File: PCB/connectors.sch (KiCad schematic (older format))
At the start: 54 parts, among them J10 70543-0002, J11 70543-0002, J12 70543-0002, J13 70543-0002, J14 Conn_02x05_Odd_Even, J15 Conn_02x05_Odd_Even, J16 70543-0001, J17 70543-0001, J18 70543-0001, J19 Conn_02x05_Odd_Even, J20 62201021121, J21 70543-0001, J22 70543-0001, J7 USB_B, J8 70543-0002, J9 70543-0002, U10 TXB0108PWR, U11 TXB0108PWR, U12 TXB0108PWR, U13 TXB0108PWR

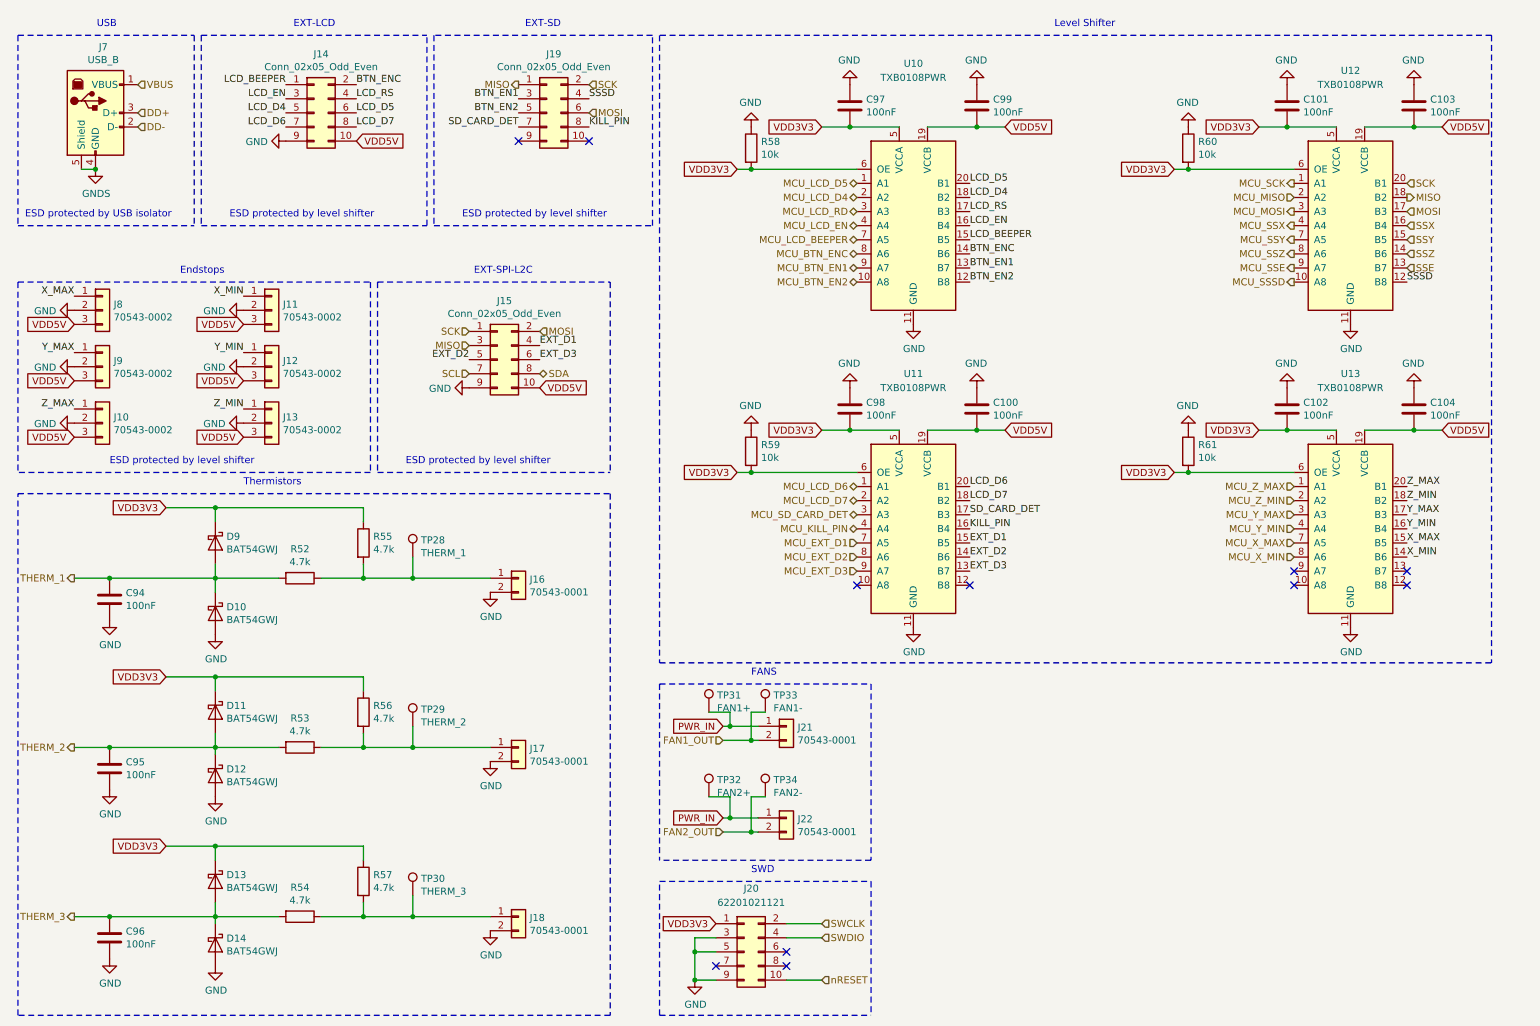
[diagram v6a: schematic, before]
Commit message: Saving work in progress.
Every component now has a 3D mode.
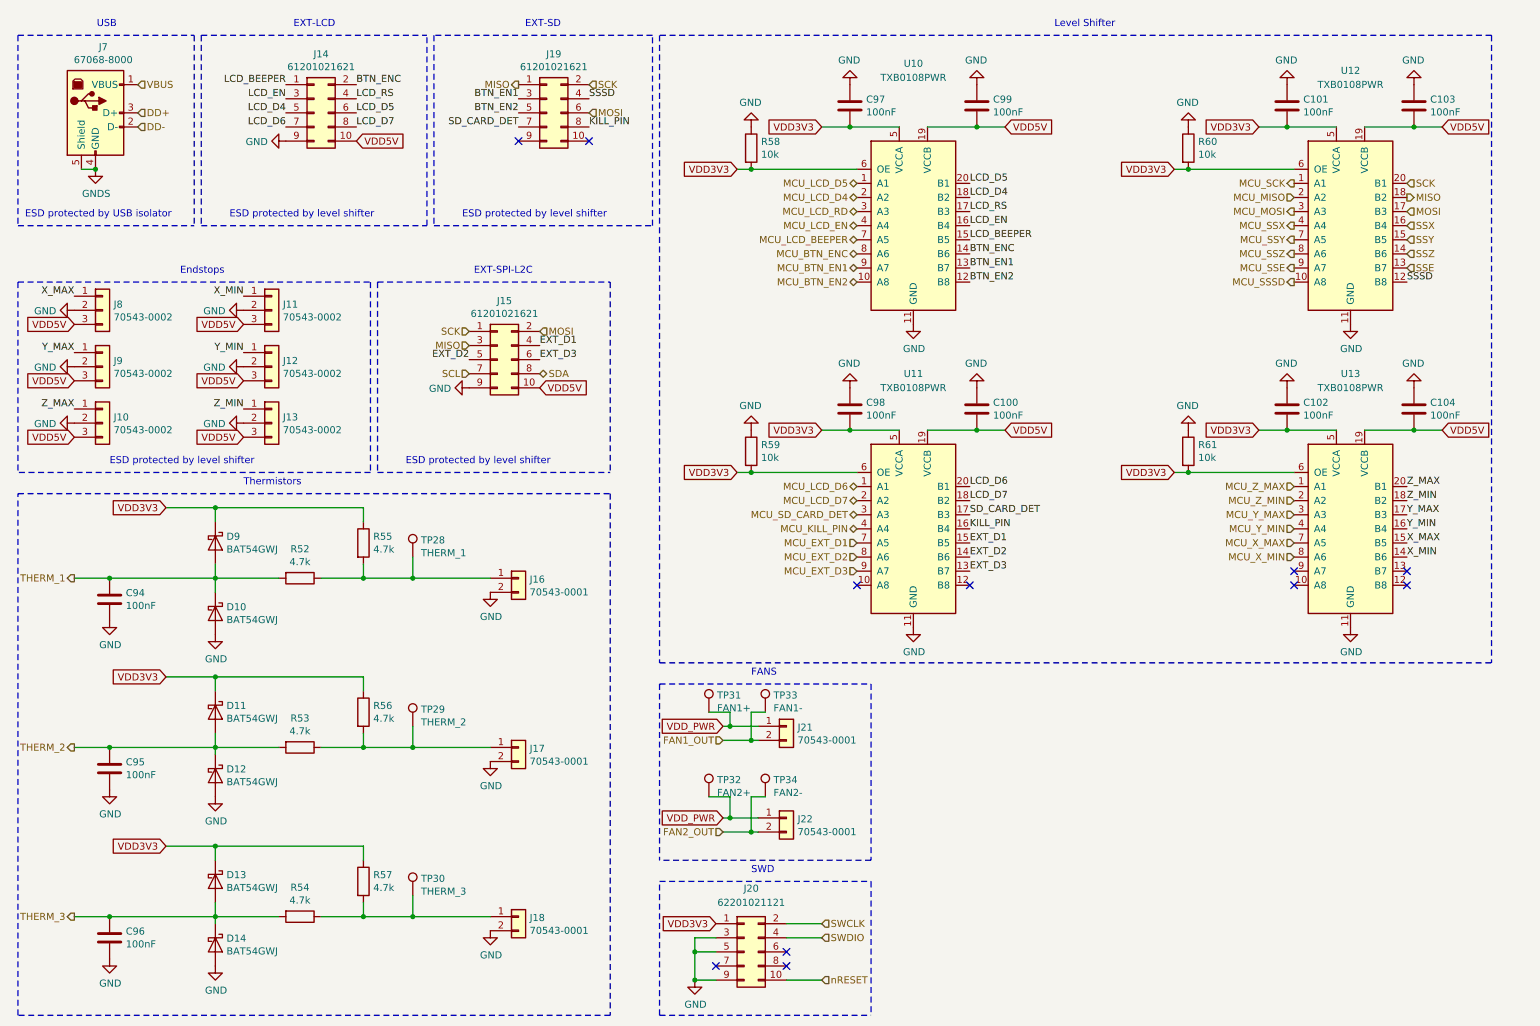
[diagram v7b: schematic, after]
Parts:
- J10, J11, J12, J13, J8, J9: footprint Connector_PinHeader_2.54mm:PinHeader_1x03_P2.54mm_Vertical -> custom-footprints:70543-0002
- J14, J15, J19: value Conn_02x05_Odd_Even -> 61201021621; footprint Connector_PinHeader_2.54mm:PinHeader_2x05_P2.54mm_Vertical -> custom-footprints:Box_Header_2x05x2.54mm_Straight
- J16, J17, J18, J21, J22: footprint Connector_PinHeader_2.54mm:PinHeader_1x02_P2.54mm_Vertical -> custom-footprints:70543-0001
- J7: value USB_B -> 67068-8000; footprint Connector_USB:USB_B_TE_5787834_Vertical -> custom-footprints:67068-8000
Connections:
- net PWR_IN renamed VDD_PWR
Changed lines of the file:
@@
 P 1150 1300
 F 0 "J7" H 1205 1767 50  0000 C CNN
-F 1 "USB_B" H 1205 1676 50  0000 C CNN
-F 2 "Connector_USB:USB_B_TE_5787834_Vertical" H 1300 1250 50  0001 C CNN
-F 3 "https://www.mouser.de/ProductDetail/TE-Connectivity/5787834-1?qs=sGAEpiMZZMulM8LPOQ%252bykzAp4yt8IxVbCJriWtalJzg%3d" H 1300 1250 50  0001 C CNN
+F 1 "67068-8000" H 1205 1676 50  0000 C CNN
+F 2 "custom-footprints:67068-8000" H 1300 1250 50  0001 C CNN
+F 3 "https://www.mouser.de/datasheet/2/276/0670688000_IO_CONNECTORS-172066.pdf" H 1300 1250 50  0001 C CNN
 	1    1150 1300
 	1    0    0    -1
@@
 P 2700 1300
 F 0 "J14" H 2750 1717 50  0000 C CNN
-F 1 "Conn_02x05_Odd_Even" H 2750 1626 50  0000 C CNN
-F 2 "Connector_PinHeader_2.54mm:PinHeader_2x05_P2.54mm_Vertical" H 2700 1300 50  0001 C CNN
-F 3 "~" H 2700 1300 50  0001 C CNN
+F 1 "61201021621" H 2750 1626 50  0000 C CNN
+F 2 "custom-footprints:Box_Header_2x05x2.54mm_Straight" H 2700 1300 50  0001 C CNN
+F 3 "https://www.mouser.de/ProductDetail/Wurth-Electronics/61201021621?qs=%2fha2pyFadugkhyfdWLPRIwz9kroMfF%252bXZWEETFcVSqiQRaqHzEC2RQ%3d%3d" H 2700 1300 50  0001 C CNN
 	1    2700 1300
 	1    0    0    -1
@@
 P 4350 1300
 F 0 "J19" H 4400 1717 50  0000 C CNN
-F 1 "Conn_02x05_Odd_Even" H 4400 1626 50  0000 C CNN
-F 2 "Connector_PinHeader_2.54mm:PinHeader_2x05_P2.54mm_Vertical" H 4350 1300 50  0001 C CNN
-F 3 "~" H 4350 1300 50  0001 C CNN
+F 1 "61201021621" H 4400 1626 50  0000 C CNN
+F 2 "custom-footprints:Box_Header_2x05x2.54mm_Straight" H 4350 1300 50  0001 C CNN
+F 3 "https://www.mouser.de/ProductDetail/Wurth-Electronics/61201021621?qs=%2fha2pyFadugkhyfdWLPRIwz9kroMfF%252bXZWEETFcVSqiQRaqHzEC2RQ%3d%3d" H 4350 1300 50  0001 C CNN
 	1    4350 1300
 	1    0    0    -1
@@
 P 4000 3050
 F 0 "J15" H 4050 3467 50  0000 C CNN
-F 1 "Conn_02x05_Odd_Even" H 4050 3376 50  0000 C CNN
-F 2 "Connector_PinHeader_2.54mm:PinHeader_2x05_P2.54mm_Vertical" H 4000 3050 50  0001 C CNN
-F 3 "~" H 4000 3050 50  0001 C CNN
+F 1 "61201021621" H 4050 3376 50  0000 C CNN
+F 2 "custom-footprints:Box_Header_2x05x2.54mm_Straight" H 4000 3050 50  0001 C CNN
+F 3 "https://www.mouser.de/ProductDetail/Wurth-Electronics/61201021621?qs=%2fha2pyFadugkhyfdWLPRIwz9kroMfF%252bXZWEETFcVSqiQRaqHzEC2RQ%3d%3d" H 4000 3050 50  0001 C CNN
 	1    4000 3050
 	1    0    0    -1
@@
 F 0 "J16" H 4229 4592 50  0000 L CNN
 F 1 "70543-0001" H 4229 4501 50  0000 L CNN
-F 2 "Connector_PinHeader_2.54mm:PinHeader_1x02_P2.54mm_Vertical" H 4150 4600 50  0001 C CNN
+F 2 "custom-footprints:70543-0001" H 4150 4600 50  0001 C CNN
 F 3 "https://www.mouser.de/ProductDetail/Molex/50-57-9402?qs=%2fha2pyFadujDsSJKPzBRyOySofHgnbNURyOy7MwFkp4%3d" H 4150 4600 50  0001 C CNN
 	1    4150 4600
@@
 F 0 "J17" H 4229 5792 50  0000 L CNN
 F 1 "70543-0001" H 4229 5701 50  0000 L CNN
-F 2 "Connector_PinHeader_2.54mm:PinHeader_1x02_P2.54mm_Vertical" H 4150 5800 50  0001 C CNN
+F 2 "custom-footprints:70543-0001" H 4150 5800 50  0001 C CNN
 F 3 "https://www.mouser.de/ProductDetail/Molex/50-57-9402?qs=%2fha2pyFadujDsSJKPzBRyOySofHgnbNURyOy7MwFkp4%3d" H 4150 5800 50  0001 C CNN
 	1    4150 5800
@@
 F 0 "J18" H 4229 6992 50  0000 L CNN
 F 1 "70543-0001" H 4229 6901 50  0000 L CNN
-F 2 "Connector_PinHeader_2.54mm:PinHeader_1x02_P2.54mm_Vertical" H 4150 7000 50  0001 C CNN
+F 2 "custom-footprints:70543-0001" H 4150 7000 50  0001 C CNN
 F 3 "https://www.mouser.de/ProductDetail/Molex/50-57-9402?qs=%2fha2pyFadujDsSJKPzBRyOySofHgnbNURyOy7MwFkp4%3d" H 4150 7000 50  0001 C CNN
 	1    4150 7000
@@
 F 0 "J8" H 1279 2742 50  0000 L CNN
 F 1 "70543-0002" H 1279 2651 50  0000 L CNN
-F 2 "Connector_PinHeader_2.54mm:PinHeader_1x03_P2.54mm_Vertical" H 1200 2700 50  0001 C CNN
+F 2 "custom-footprints:70543-0002" H 1200 2700 50  0001 C CNN
 F 3 "~" H 1200 2700 50  0001 C CNN
 	1    1200 2700
@@
 F 0 "J11" H 2479 2742 50  0000 L CNN
 F 1 "70543-0002" H 2479 2651 50  0000 L CNN
-F 2 "Connector_PinHeader_2.54mm:PinHeader_1x03_P2.54mm_Vertical" H 2400 2700 50  0001 C CNN
+F 2 "custom-footprints:70543-0002" H 2400 2700 50  0001 C CNN
 F 3 "~" H 2400 2700 50  0001 C CNN
 	1    2400 2700
@@
 F 0 "J9" H 1279 3142 50  0000 L CNN
 F 1 "70543-0002" H 1279 3051 50  0000 L CNN
-F 2 "Connector_PinHeader_2.54mm:PinHeader_1x03_P2.54mm_Vertical" H 1200 3100 50  0001 C CNN
+F 2 "custom-footprints:70543-0002" H 1200 3100 50  0001 C CNN
 F 3 "~" H 1200 3100 50  0001 C CNN
 	1    1200 3100
@@
 F 0 "J12" H 2479 3142 50  0000 L CNN
 F 1 "70543-0002" H 2479 3051 50  0000 L CNN
-F 2 "Connector_PinHeader_2.54mm:PinHeader_1x03_P2.54mm_Vertical" H 2400 3100 50  0001 C CNN
+F 2 "custom-footprints:70543-0002" H 2400 3100 50  0001 C CNN
 F 3 "~" H 2400 3100 50  0001 C CNN
 	1    2400 3100
@@
 F 0 "J10" H 1279 3542 50  0000 L CNN
 F 1 "70543-0002" H 1279 3451 50  0000 L CNN
-F 2 "Connector_PinHeader_2.54mm:PinHeader_1x03_P2.54mm_Vertical" H 1200 3500 50  0001 C CNN
+F 2 "custom-footprints:70543-0002" H 1200 3500 50  0001 C CNN
 F 3 "~" H 1200 3500 50  0001 C CNN
 	1    1200 3500
@@
 F 0 "J13" H 2479 3542 50  0000 L CNN
 F 1 "70543-0002" H 2479 3451 50  0000 L CNN
-F 2 "Connector_PinHeader_2.54mm:PinHeader_1x03_P2.54mm_Vertical" H 2400 3500 50  0001 C CNN
+F 2 "custom-footprints:70543-0002" H 2400 3500 50  0001 C CNN
 F 3 "~" H 2400 3500 50  0001 C CNN
 	1    2400 3500
@@
 F 0 "J21" H 6129 5642 50  0000 L CNN
 F 1 "70543-0001" H 6129 5551 50  0000 L CNN
-F 2 "Connector_PinHeader_2.54mm:PinHeader_1x02_P2.54mm_Vertical" H 6050 5650 50  0001 C CNN
+F 2 "custom-footprints:70543-0001" H 6050 5650 50  0001 C CNN
 F 3 "https://www.mouser.de/ProductDetail/Molex/50-57-9402?qs=%2fha2pyFadujDsSJKPzBRyOySofHgnbNURyOy7MwFkp4%3d" H 6050 5650 50  0001 C CNN
 	1    6050 5650
@@
 FAN1_OUT
 Text GLabel 5600 5650 0    50   Input ~ 0
-PWR_IN
+VDD_PWR
 $Comp
 L Connector_Generic:Conn_01x02 J22
@@
 F 0 "J22" H 6129 6292 50  0000 L CNN
 F 1 "70543-0001" H 6129 6201 50  0000 L CNN
-F 2 "Connector_PinHeader_2.54mm:PinHeader_1x02_P2.54mm_Vertical" H 6050 6300 50  0001 C CNN
+F 2 "custom-footprints:70543-0001" H 6050 6300 50  0001 C CNN
 F 3 "https://www.mouser.de/ProductDetail/Molex/50-57-9402?qs=%2fha2pyFadujDsSJKPzBRyOySofHgnbNURyOy7MwFkp4%3d" H 6050 6300 50  0001 C CNN
 	1    6050 6300
@@
 FAN2_OUT
 Text GLabel 5600 6300 0    50   Input ~ 0
-PWR_IN
+VDD_PWR
 Wire Notes Line
 	6650 6600 5150 6600

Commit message: Removed logic level converter. Changed LDO.
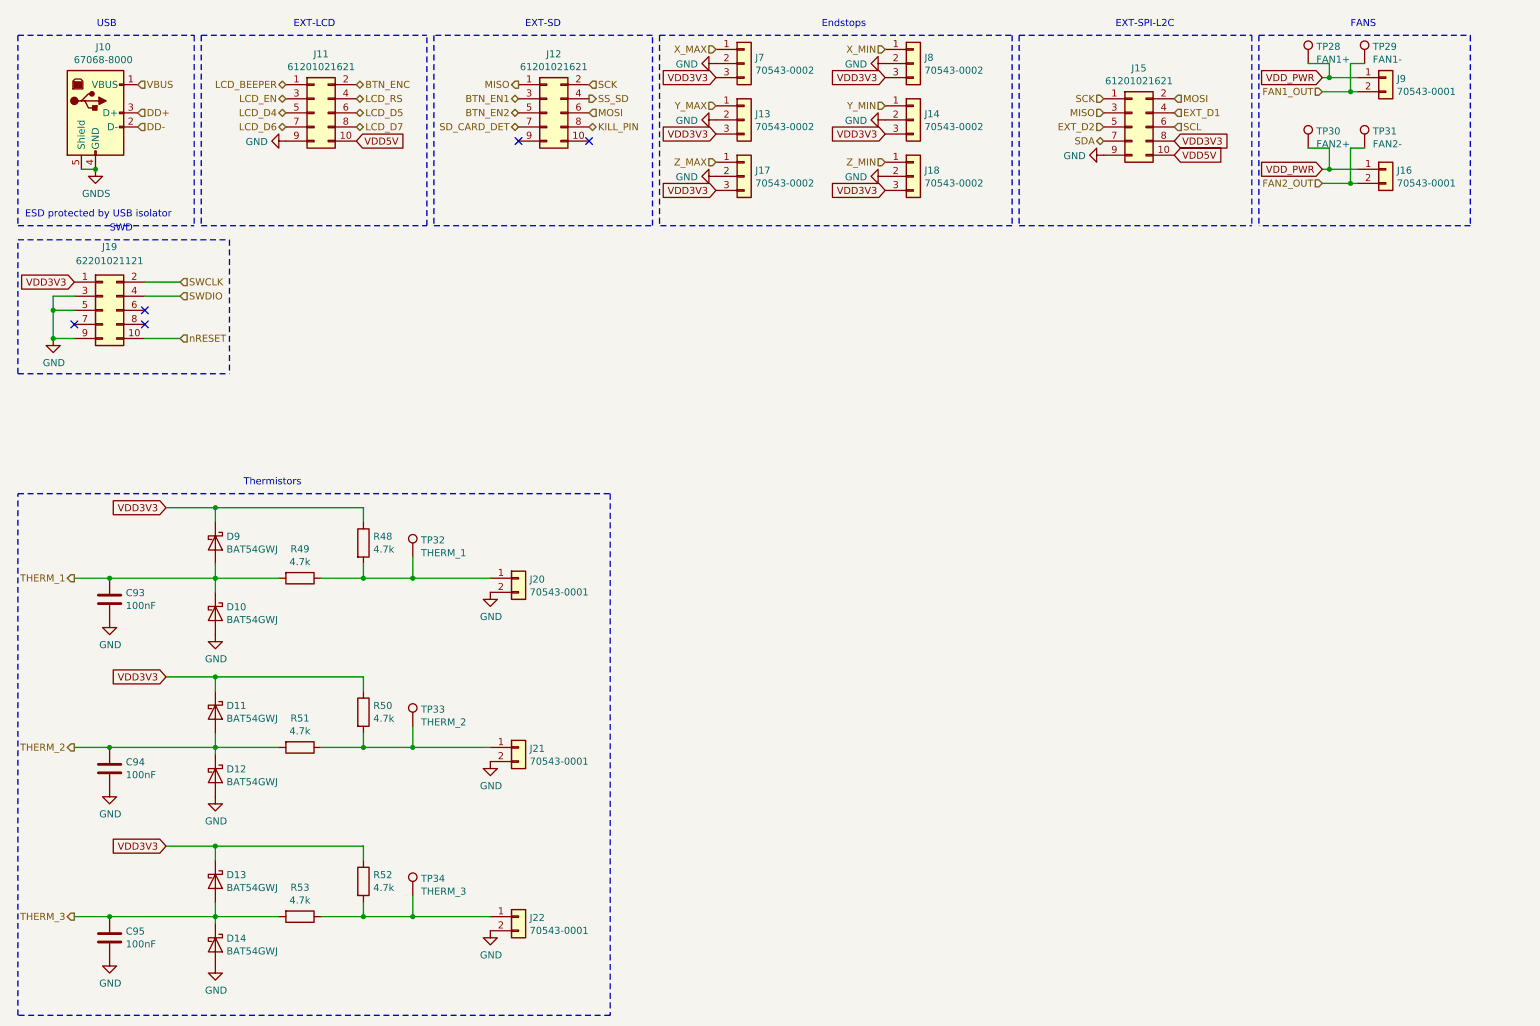
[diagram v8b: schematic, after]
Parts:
- removed C100, C101, C102, C103, C104, C97, C98, C99: 100nF, Capacitor_SMD:C_0603_1608Metric, symbol Device:C
- removed R58, R59, R60, R61: 10k, Resistor_SMD:R_0603_1608Metric, symbol Device:R
- removed U10, U11, U12, U13: TXB0108PWR, Package_SO:TSSOP-20_4.4x6.5mm_P0.65mm, symbol Logic_LevelTranslator:TXB0108DQSR
- renumbered C94 to C93, C95 to C94, C96 to C95, J7 to J10, J14 to J11, J19 to J12, J9 to J13, J12 to J14, J22 to J16, J10 to J17, J13 to J18, J20 to J19, J16 to J20, J17 to J21, J18 to J22, J8 to J7, J11 to J8, J21 to J9, R55 to R48, R52 to R49, R56 to R50, R53 to R51, R57 to R52, R54 to R53, TP31 to TP28, TP33 to TP29, TP32 to TP30, TP34 to TP31, TP28 to TP32, TP29 to TP33, TP30 to TP34
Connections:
- net EXT_D3 is gone; now on net SCL: J15.6 (Pin_6)
- net SCL: no longer J15.7 (Pin_7)
- net SDA: now also J15.7 (Pin_7); no longer J15.8 (Pin_8)
- net VDD3V3: now also J13.3 (Pin_3), J14.3 (Pin_3), J15.8 (Pin_8), J17.3 (Pin_3), J18.3 (Pin_3), J7.3 (Pin_3), J8.3 (Pin_3)
- net VDD5V: no longer J13.3 (Pin_3), J14.3 (Pin_3), J17.3 (Pin_3), J18.3 (Pin_3), J7.3 (Pin_3), J8.3 (Pin_3)
- net SSSD renamed SS_SD
- no-connect marks 11 -> 5
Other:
- note removed: "ESD protected by level shifter"
- note removed: "Level Shifter"
- moved on the sheet: J13, J14, J15, J16, J17, J18, J19, J7, J8, J9, TP28, TP29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
